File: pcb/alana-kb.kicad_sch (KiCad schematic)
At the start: 1 part, among them U1 STM32F072CBUx

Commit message: usb c, power, mcu
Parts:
- removed U1: STM32F072CBUx, Package_DFN_QFN:QFN-48-1EP_7x7mm_P0.5mm_EP5.6x5.6mm, symbol library:STM32F072CBUx
- added C10, C11: 1uF, Capacitor_SMD:C_0402_1005Metric, symbol Device:C
- added FID1, FID2: Fiducial, Fiducial:Fiducial_0.75mm_Mask1.5mm, symbol Mechanical:Fiducial
- added U3: AP2112K-3.3TRG1, Package_TO_SOT_SMD:SOT-23-5, symbol library:AP2112K-3.3TRG1
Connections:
- net GND: now also C10.2, C11.2, U3.2 (GND)
- new net 3V3: C11.1, U3.5 (VOUT)
- new net 5V0: C10.1, U3.1 (VIN), U3.3 (EN)
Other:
- added sheet STM32 (stm32.kicad_sch)
- added sheet USB C (usb.kicad_sch)

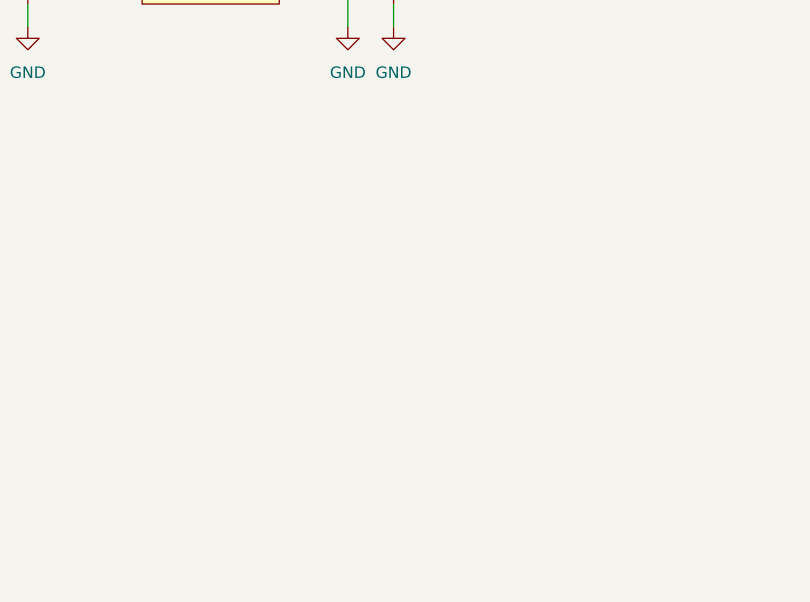
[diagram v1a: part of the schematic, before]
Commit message: cleanup, add kb matrix
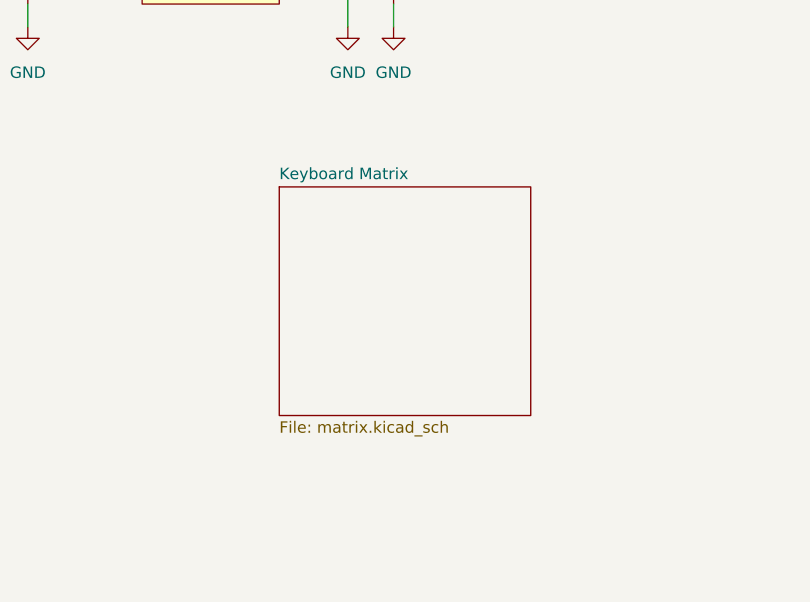
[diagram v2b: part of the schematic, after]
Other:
- added sheet Keyboard Matrix (matrix.kicad_sch)
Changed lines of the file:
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@@
+		)
+	)
+	(sheet
+		(at 129.54 114.3)
+		(size 27.94 25.4)
+		(exclude_from_sim no)
+		(in_bom yes)
+		(on_board yes)
+		(dnp no)
+		(fields_autoplaced yes)
+		(stroke
+			(width 0.1524)
+			(type solid)
+		)
+		(fill
+			(color 0 0 0 0.0000)
+		)
+		(property "Sheetname" "Keyboard Matrix"
+			(at 129.54 113.5884 0)
+			(effects
+				(font
+					(size 1.27 1.27)
+				)
+				(justify left bottom)
+			)
+		)
+		(property "Sheetfile" "matrix.kicad_sch"
+			(at 129.54 140.2846 0)
+			(effects
+				(font
+					(size 1.27 1.27)
+				)
+				(justify left top)
+			)
+		)
+		(instances
+			(project "alana-kb"
+				(path "/14664179-4b45-478a-8e33-e1eaac937d3d"
+					(page "4")
+				)
+			)
 		)
 	)

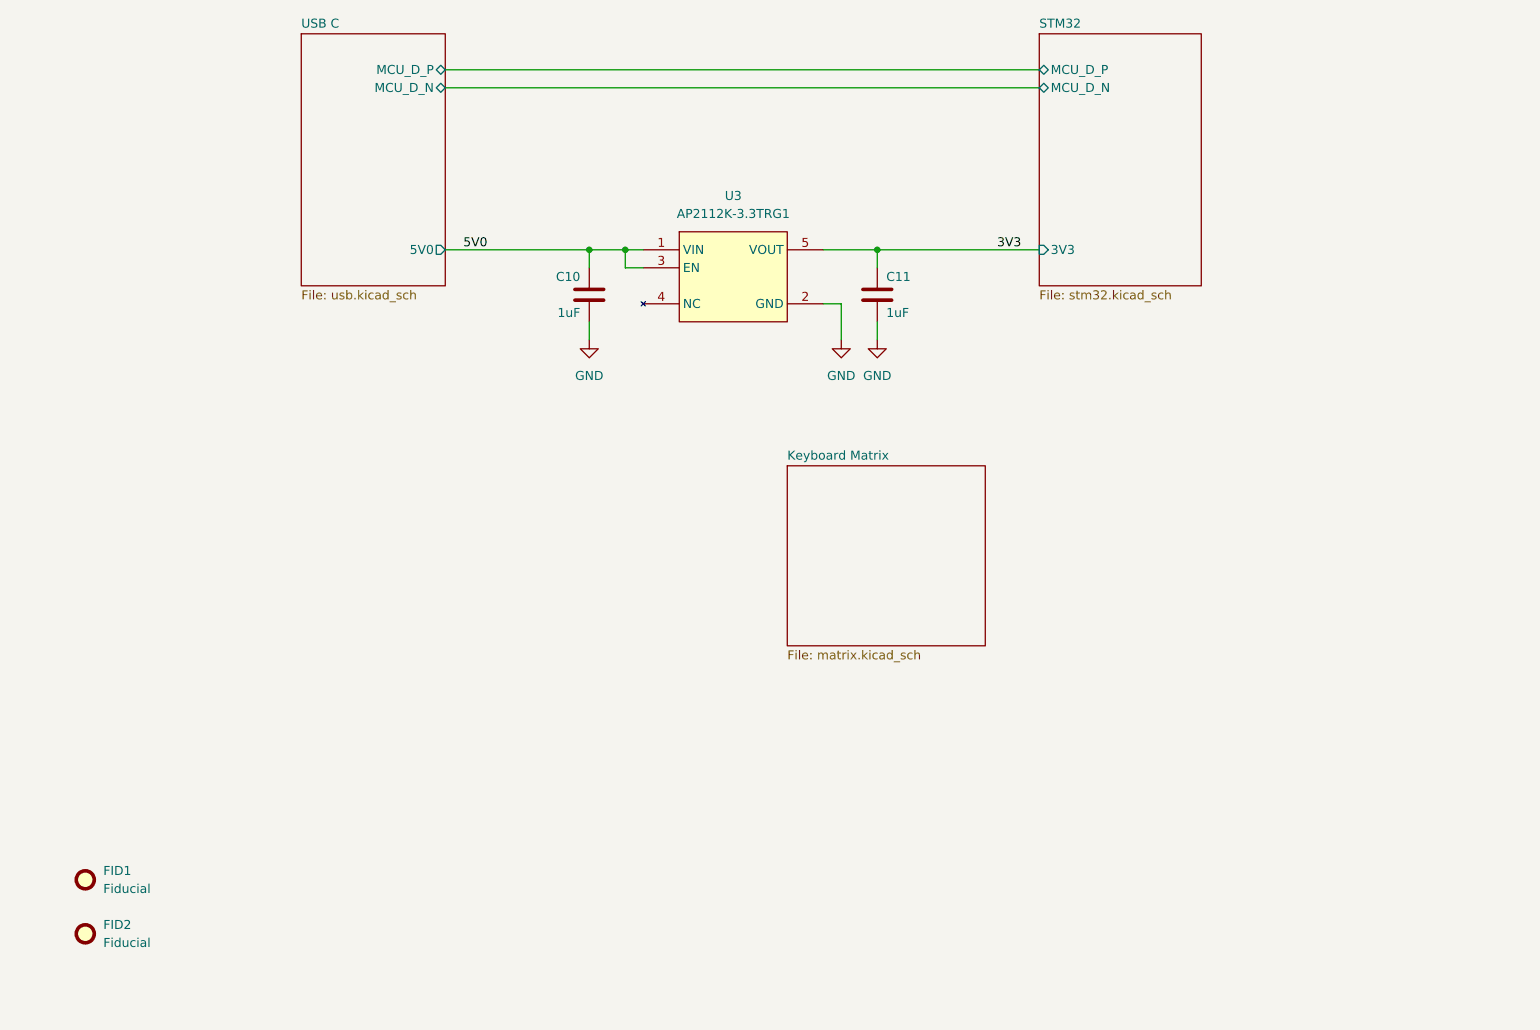
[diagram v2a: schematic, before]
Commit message: kb matrix complete, stm32 wiring done
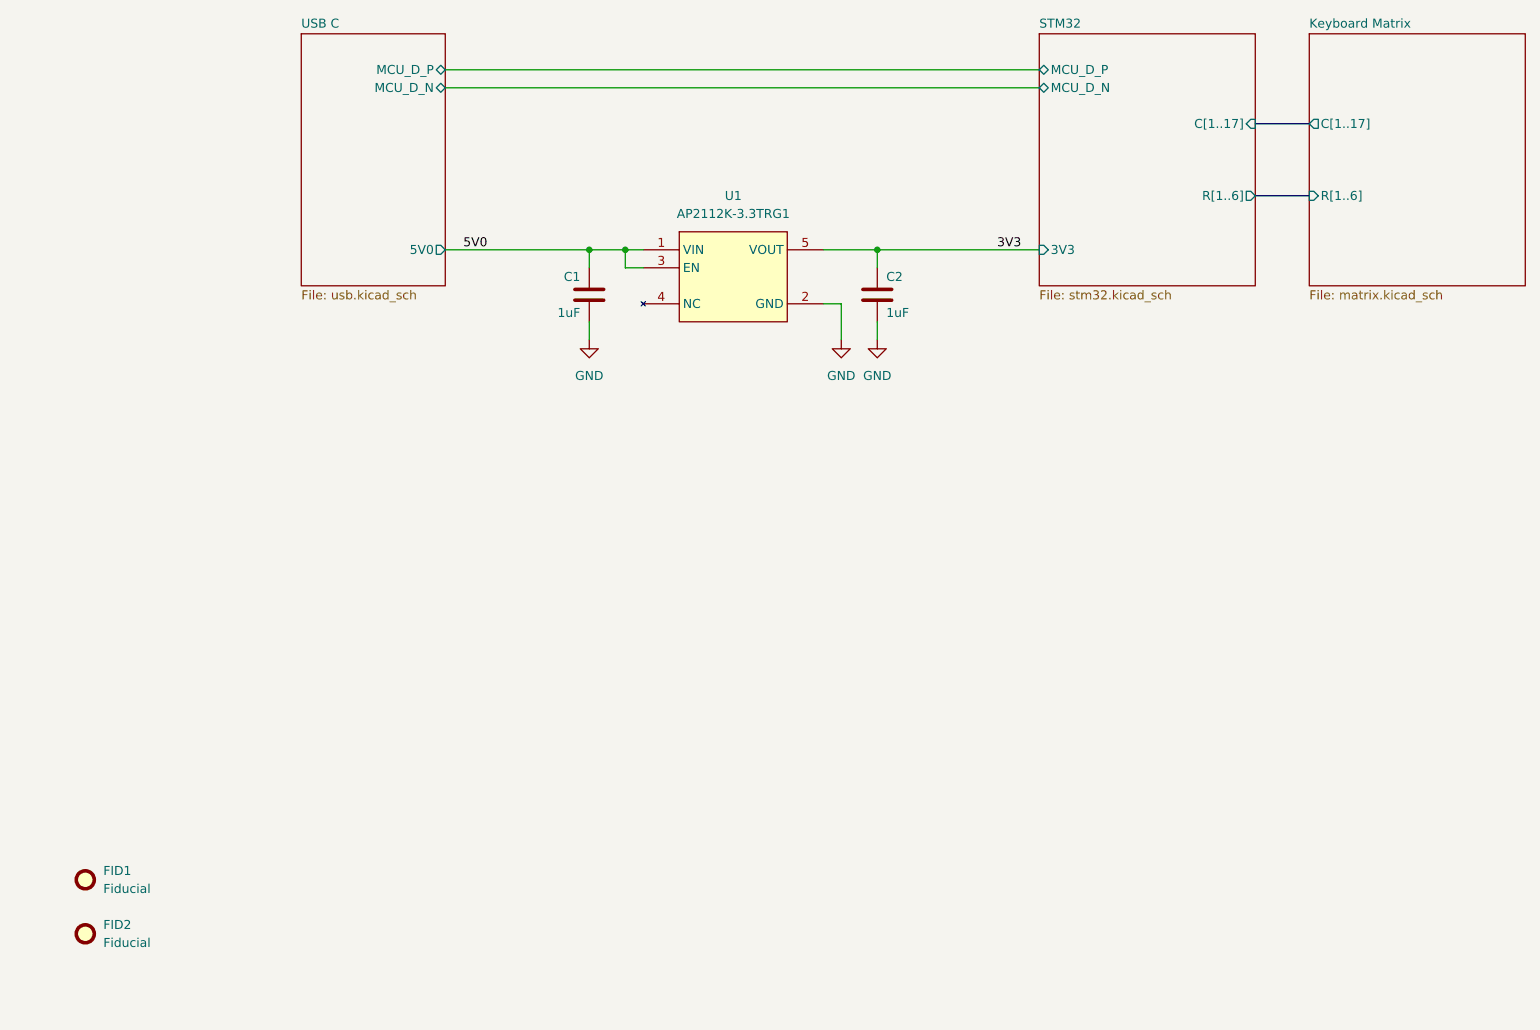
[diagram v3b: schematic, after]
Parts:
- renumbered C10 to C1, C11 to C2, U3 to U1
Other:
- sheet Keyboard Matrix ports: added C[1..17], R[1..6]; removed none
- sheet STM32 ports: added C[1..17], R[1..6]; removed none
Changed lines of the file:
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@@
+		)
+	)
+	(bus
+		(pts
+			(xy 195.58 66.04) (xy 203.2 66.04)
+		)
+		(stroke
+			(width 0)
+			(type default)
 		)
 	)
@@
 		(pts
 			(xy 142.24 83.82) (xy 142.24 86.36)
+		)
+		(stroke
+			(width 0)
+			(type default)
+		)
+	)
+	(bus
+		(pts
+			(xy 195.58 76.2) (xy 203.2 76.2)
 		)
 		(stroke
@@
 		(dnp no)
 		(fields_autoplaced yes)
-		(property "Reference" "U3"
+		(property "Reference" "U1"
 			(at 121.92 76.2 0)
 			(effects
@@
 			(project ""
 				(path "/14664179-4b45-478a-8e33-e1eaac937d3d"
-					(reference "U3")
+					(reference "U1")
 					(unit 1)
 				)
@@
 		(dnp no)
 		(fields_autoplaced yes)
-		(property "Reference" "#PWR017"
+		(property "Reference" "#PWR02"
 			(at 137.16 102.87 0)
 			(effects
@@
 			(project "alana-kb"
 				(path "/14664179-4b45-478a-8e33-e1eaac937d3d"
-					(reference "#PWR017")
+					(reference "#PWR02")
 					(unit 1)
 				)
@@
 		(on_board yes)
 		(dnp no)
-		(property "Reference" "C11"
+		(property "Reference" "C2"
 			(at 143.51 87.63 0)
 			(effects
@@
 			(project "alana-kb"
 				(path "/14664179-4b45-478a-8e33-e1eaac937d3d"
-					(reference "C11")
+					(reference "C2")
 					(unit 1)
 				)
@@
 		(dnp no)
 		(fields_autoplaced yes)
-		(property "Reference" "#PWR016"
+		(property "Reference" "#PWR01"
 			(at 101.6 102.87 0)
 			(effects
@@
 			(project ""
 				(path "/14664179-4b45-478a-8e33-e1eaac937d3d"
-					(reference "#PWR016")
+					(reference "#PWR01")
 					(unit 1)
 				)
@@
 		(on_board yes)
 		(dnp no)
-		(property "Reference" "C10"
+		(property "Reference" "C1"
 			(at 100.33 87.63 0)
 			(effects
@@
 			(project "alana-kb"
 				(path "/14664179-4b45-478a-8e33-e1eaac937d3d"
-					(reference "C10")
+					(reference "C1")
 					(unit 1)
 				)
@@
 		(dnp no)
 		(fields_autoplaced yes)
-		(property "Reference" "#PWR018"
+		(property "Reference" "#PWR03"
 			(at 142.24 102.87 0)
 			(effects
@@
 			(project "alana-kb"
 				(path "/14664179-4b45-478a-8e33-e1eaac937d3d"
-					(reference "#PWR018")
+					(reference "#PWR03")
 					(unit 1)
 				)
@@
 	(sheet
 		(at 165.1 53.34)
-		(size 22.86 35.56)
+		(size 30.48 35.56)
 		(exclude_from_sim no)
 		(in_bom yes)
@@
 				)
 				(justify left)
+			)
+		)
+		(pin "C[1..17]" input
+			(at 195.58 66.04 0)
+			(effects
+				(font
+					(size 1.27 1.27)
+				)
+				(justify right)
+			)
+		)
+		(pin "R[1..6]" output
+			(at 195.58 76.2 0)
+			(effects
+				(font
+					(size 1.27 1.27)
+				)
+				(justify right)
 			)
 		)
@@
 	)
 	(sheet
-		(at 129.54 114.3)
-		(size 27.94 25.4)
+		(at 203.2 53.34)
+		(size 30.48 35.56)
 		(exclude_from_sim no)
 		(in_bom yes)
@@
 		)
 		(property "Sheetname" "Keyboard Matrix"
-			(at 129.54 113.5884 0)
+			(at 203.2 52.6284 0)
 			(effects
 				(font
@@
 		)
 		(property "Sheetfile" "matrix.kicad_sch"
-			(at 129.54 140.2846 0)
+			(at 203.2 89.4846 0)
 			(effects
 				(font
@@
 			)
 		)
+		(pin "C[1..17]" output
+			(at 203.2 66.04 180)
+			(effects
+				(font
+					(size 1.27 1.27)
+				)
+				(justify left)
+			)
+		)
+		(pin "R[1..6]" input
+			(at 203.2 76.2 180)
+			(effects
+				(font
+					(size 1.27 1.27)
+				)
+				(justify left)
+			)
+		)

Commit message: replaced usb c with molex for udb
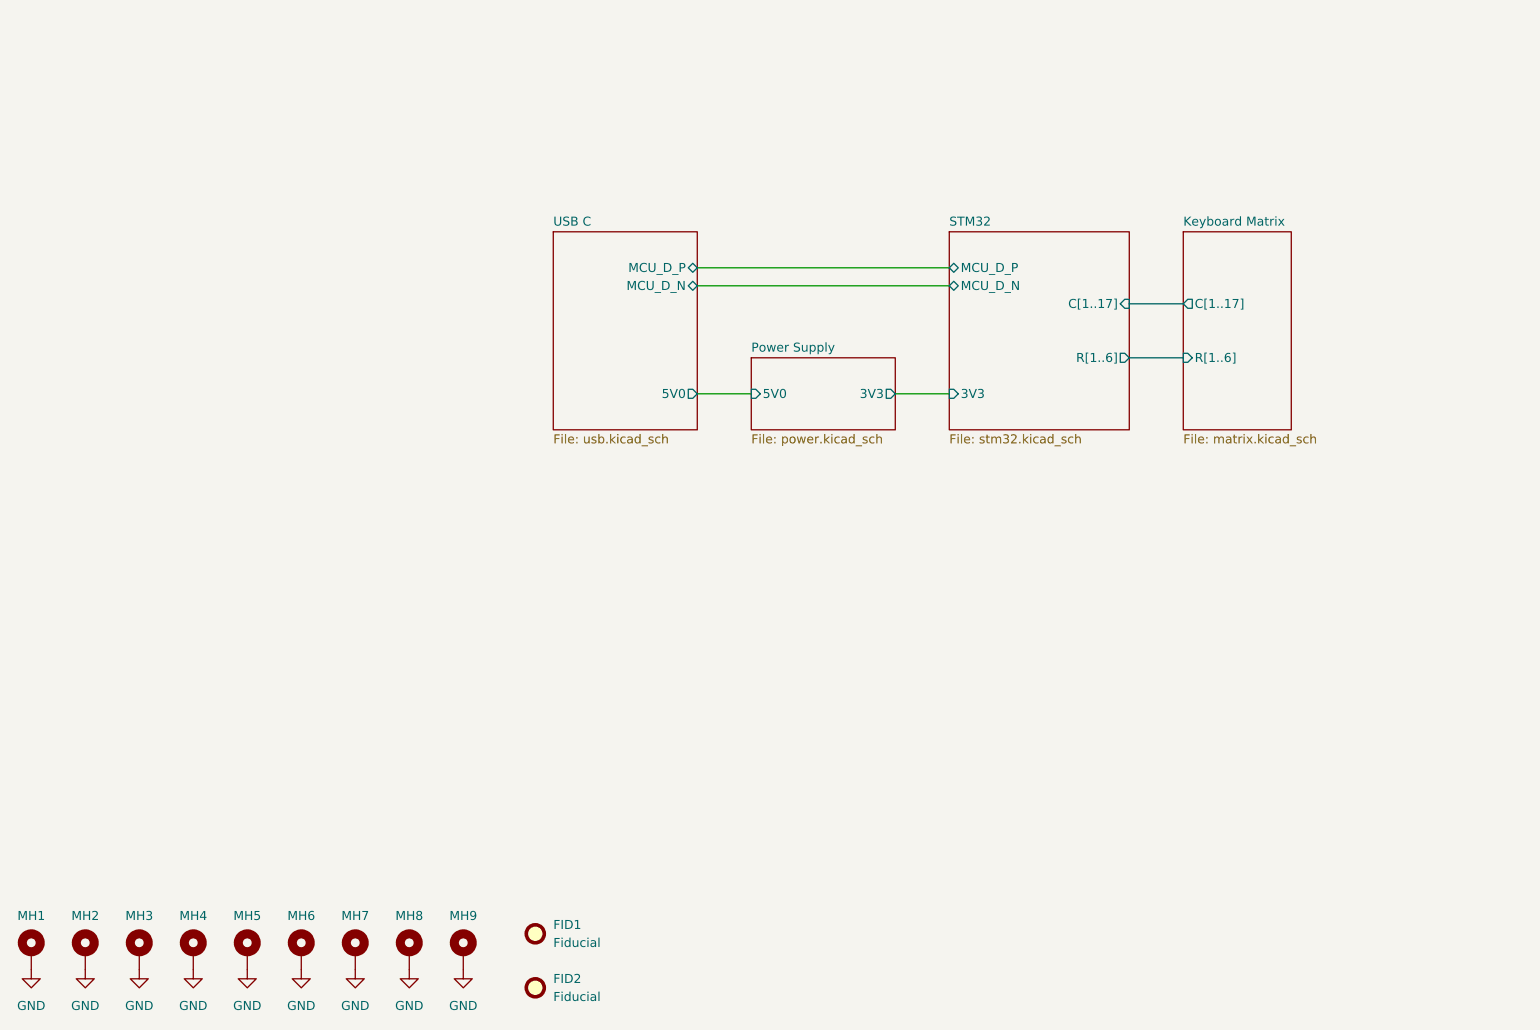
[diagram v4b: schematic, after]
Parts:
- removed C1, C2: 1uF, Capacitor_SMD:C_0402_1005Metric, symbol Device:C
- removed U1: AP2112K-3.3TRG1, Package_TO_SOT_SMD:SOT-23-5, symbol library:AP2112K-3.3TRG1
- added MH1, MH2, MH3, MH4, MH5, MH6, MH7, MH8, MH9: MountingHole_Pad, MountingHole:MountingHole_2.2mm_M2_ISO7380_Pad, symbol Mechanical:MountingHole_Pad
- FID1, FID2: footprint Fiducial:Fiducial_0.75mm_Mask1.5mm -> Fiducial:Fiducial_1.5mm_Mask4.5mm
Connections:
- net GND: now also MH1.1, MH2.1, MH3.1, MH4.1, MH5.1, MH6.1, MH7.1, MH8.1, MH9.1
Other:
- added sheet Power Supply (power.kicad_sch)
- moved on the sheet: FID1, FID2

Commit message: reroute matrix
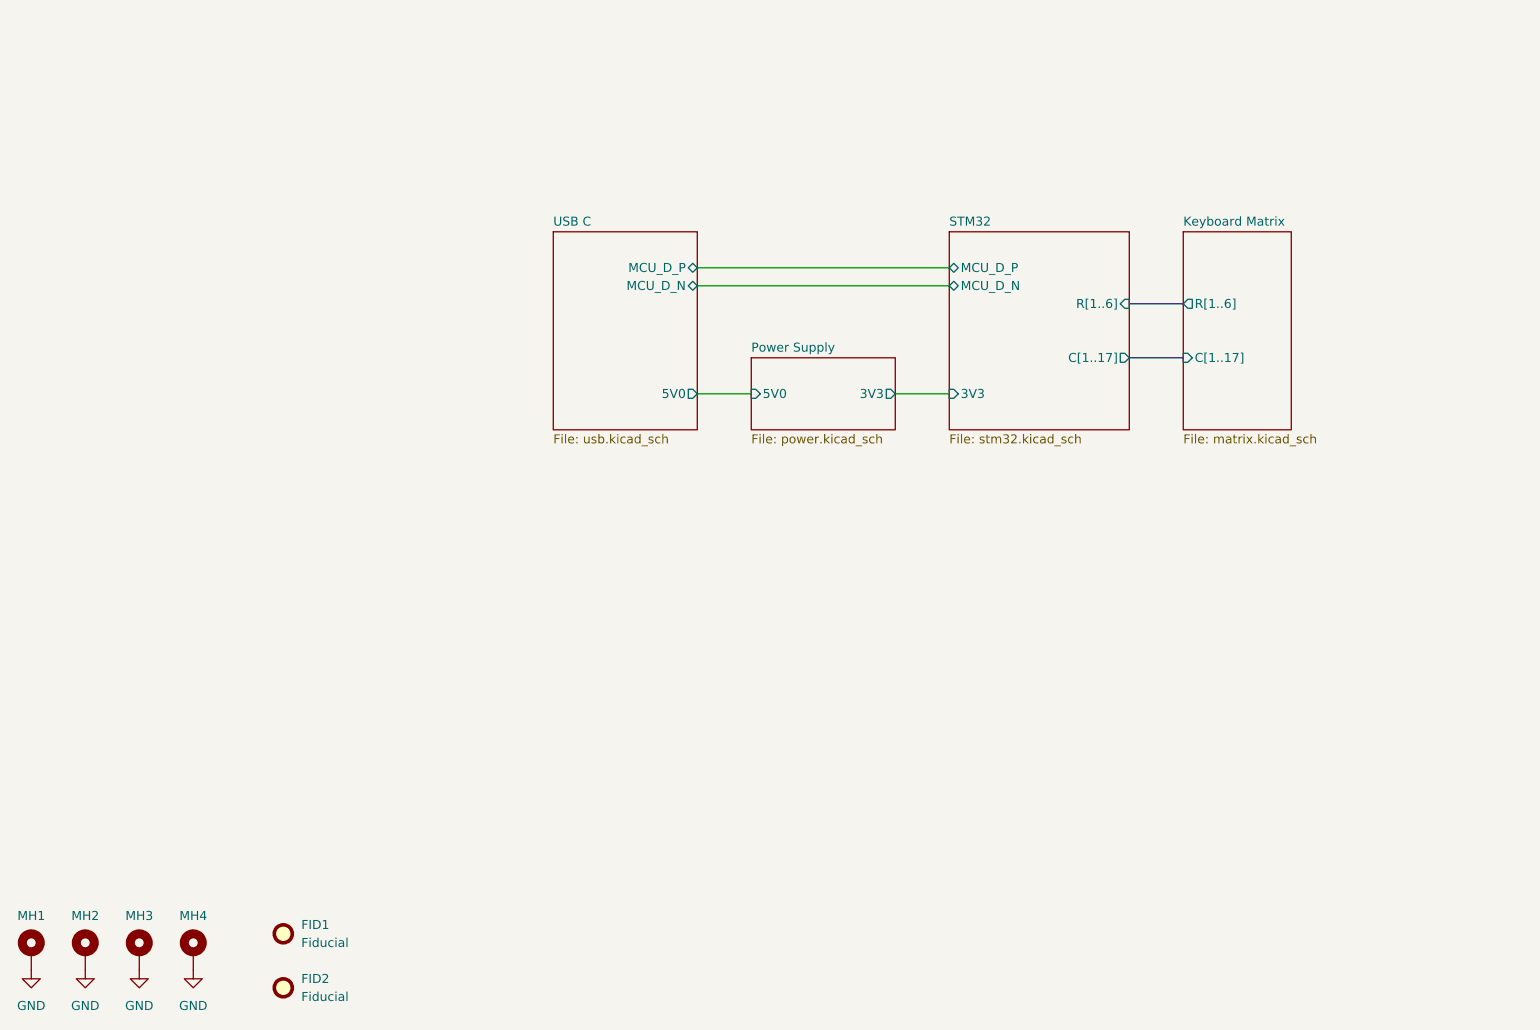
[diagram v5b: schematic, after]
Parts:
- removed MH5, MH6, MH7, MH8, MH9: MountingHole_Pad, MountingHole:MountingHole_2.2mm_M2_ISO7380_Pad, symbol Mechanical:MountingHole_Pad
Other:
- company: (none) -> ASE, ASW, AMB
- title: (none) -> ALANA-KB PCB
- moved on the sheet: FID1, FID2
